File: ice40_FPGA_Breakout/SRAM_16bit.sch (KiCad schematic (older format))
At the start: 23 parts

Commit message: post review fix
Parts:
- added R?: 0, symbol R
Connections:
- net FLASH_~WP: now also R?.1; no longer R?.2, U?.3 (~WP)
- new net: R?.2, R?.2, U?.3 (~WP)
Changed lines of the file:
@@
 $EndComp
 Wire Wire Line
-	9800 3300 10100 3300
-Wire Wire Line
-	7450 3400 7950 3400
+	9800 3300 9950 3300
+Wire Wire Line
+	9950 3300 10100 3300
+Wire Wire Line
+	7450 3400 7700 3400
+Wire Wire Line
+	7700 3400 7850 3400
+Wire Wire Line
+	7850 3400 7950 3400
 Wire Wire Line
 	7550 3000 7550 3200
@@
 	7850 2550 7850 2700
 Wire Wire Line
-	7550 2550 10650 2550
+	7550 2550 7700 2550
+Wire Wire Line
+	7700 2550 7850 2550
+Wire Wire Line
+	7850 2550 9950 2550
+Wire Wire Line
+	9950 2550 10100 2550
+Wire Wire Line
+	10100 2550 10300 2550
+Wire Wire Line
+	10300 2550 10550 2550
+Wire Wire Line
+	10550 2550 10650 2550
 Connection ~ 7700 2550
 Connection ~ 9950 2550
@@
 	10300 2900 10300 2950
 Wire Wire Line
-	10300 2950 10750 2950
+	10300 2950 10550 2950
+Wire Wire Line
+	10550 2950 10750 2950
 Wire Wire Line
 	10550 2950 10550 2900
@@
 Connection ~ 10550 2950
 Wire Wire Line
-	8000 1550 8750 1550
-Wire Wire Line
-	8000 1650 8750 1650
-Wire Wire Line
-	8000 1750 8750 1750
+	8000 1550 8400 1550
+Wire Wire Line
+	8400 1550 8500 1550
+Wire Wire Line
+	8500 1550 8750 1550
+Wire Wire Line
+	8000 1650 8250 1650
+Wire Wire Line
+	8250 1650 8750 1650
+Wire Wire Line
+	8000 1750 8100 1750
+Wire Wire Line
+	8100 1750 8750 1750
 Wire Wire Line
 	8400 1200 8400 1550
 Connection ~ 8400 1550
-Wire Wire Line
-	9550 1650 10150 1650
 Connection ~ 8100 1750
 Connection ~ 8250 1650
@@
 Wire Wire Line
 	8100 1200 8100 1750
-Wire Wire Line
-	9550 1550 10150 1550
 Wire Wire Line
 	9700 1200 9700 1550
@@
 	10000 800  10000 900
 Wire Wire Line
-	7750 800  10000 800
+	7750 800  8100 800
+Wire Wire Line
+	8100 800  8250 800
+Wire Wire Line
+	8250 800  8400 800
+Wire Wire Line
+	8400 800  8700 800
+Wire Wire Line
+	8700 800  9150 800
+Wire Wire Line
+	9150 800  9350 800
+Wire Wire Line
+	9350 800  9700 800
+Wire Wire Line
+	9700 800  9850 800
+Wire Wire Line
+	9850 800  10000 800
 Wire Wire Line
 	9850 800  9850 900
@@
 	1850 3600 2000 3600
 Wire Wire Line
-	9800 3200 10150 3200
-Wire Wire Line
-	9550 1750 10150 1750
+	9800 3200 9950 3200
+Wire Wire Line
+	9950 3200 10150 3200
+Wire Wire Line
+	9550 1750 10000 1750
+Wire Wire Line
+	10000 1750 10150 1750
 Wire Wire Line
 	10000 1200 10000 1750
 Wire Wire Line
-	7450 3300 7950 3300
-Wire Wire Line
-	7450 3200 7950 3200
+	7450 3300 7700 3300
+Wire Wire Line
+	7700 3300 7950 3300
+Wire Wire Line
+	7450 3200 7550 3200
+Wire Wire Line
+	7550 3200 7950 3200
 $Comp
 L GND #PWR016
@@
 Text HLabel 10150 3200 2    39   Input Italic 8
 FPGA_SS
-Text Notes 10900 3300 2    39   Italic 8
+Text Notes 8950 3000 2    39   Italic 8
 iCE SPI SS
 Text HLabel 1850 3600 0    39   Input Italic 8
@@
 Text HLabel 1850 7350 0    39   Input Italic 8
 CMOS_CLK2
-Text HLabel 750  4450 0    39   Input Italic 8
+Text HLabel 750  4450 0    39   Input ~ 0
 LED1
-Text HLabel 750  4550 0    39   Input Italic 8
+Text HLabel 750  4550 0    39   Input ~ 0
 LED2
-Text HLabel 750  4650 0    39   Input Italic 8
+Text HLabel 750  4650 0    39   Input ~ 0
 LED3
-Text HLabel 750  4750 0    39   Input Italic 8
+Text HLabel 750  4750 0    39   Input ~ 0
 LED4
-Text HLabel 750  4850 0    39   Input Italic 8
+Text HLabel 750  4850 0    39   Input ~ 0
 LED5
-Text HLabel 750  4950 0    39   Input Italic 8
+Text HLabel 750  4950 0    39   Input ~ 0
 LED6
-Text HLabel 750  5050 0    39   Input Italic 8
+Text HLabel 750  5050 0    39   Input ~ 0
 LED7
-Text HLabel 750  4350 0    39   Input Italic 8
+Text HLabel 750  4350 0    39   Input ~ 0
 LED0
 $Comp
@@
 Text HLabel 900  5300 0    39   Input ~ 0
 XTAL2_EN
-Text GLabel 10150 1550 2    39   Input ~ 0
-FLASH_~WP
-Text GLabel 10150 1650 2    39   Input ~ 0
-FLASH_~HOLD
 Text GLabel 900  5450 0    39   Input ~ 0
 FLASH_~WP
 Text GLabel 900  5550 0    39   Input ~ 0
 FLASH_~HOLD
+Text HLabel 750  5150 0    39   Input ~ 0
+LED8
+Wire Wire Line
+	9550 1650 9850 1650
+Wire Wire Line
+	9850 1650 10800 1650
+$Comp
+L R R?
+U 1 1 5A5FCC87
+P 10250 1550
+F 0 "R?" V 10330 1550 50  0000 C CNN
+F 1 "0" V 10250 1550 50  0000 C CNN
+F 2 "" V 10180 1550 50  0001 C CNN
+F 3 "" H 10250 1550 50  0001 C CNN
+	1    10250 1550
+	0    1    -1   0
+$EndComp
+Wire Wire Line
+	9550 1550 9700 1550
+Wire Wire Line
+	9700 1550 10100 1550
+Wire Wire Line
+	10400 1550 10800 1550
+Text Label 10450 1550 0    39   ~ 0
+FLASH_~WP
+Connection ~ 10800 1550
+Text Label 10400 1650 0    39   ~ 0
+FLASH_~HOLD
+Connection ~ 10800 1650
 $EndSCHEMATC

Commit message: Component Annotated and R/C/Conn/TP CVPCB mapping
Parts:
- C19: renamed from C?; value C -> 0.1uF
- C20: renamed from C?; value C -> 1uF
- C57, C74: renamed from 0.1uf; value C -> 0.1uF
- gave numbers to parts that had none: 18
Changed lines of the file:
@@
 P 8150 3050
 AR Path="/5A0778ED/5A3EF3FF" Ref="U?"  Part="6"
-AR Path="/5A07796D/5A3EF3FF" Ref="U?"  Part="6"
-F 0 "U?" H 8250 3150 60  0000 C CNN
+AR Path="/5A07796D/5A3EF3FF" Ref="U1"  Part="6"
+F 0 "U1" H 8250 3150 60  0000 C CNN
 F 1 "iCE40HX8_CT256" H 8850 3000 60  0000 C CNN
 F 2 "" H 8150 3050 60  0001 C CNN
@@
 $EndComp
 $Comp
-L iCE40HX8_CT256 U?
+L iCE40HX8_CT256 U1
 U 2 1 5A3F10D7
 P 2200 650
-F 0 "U?" H 2300 750 60  0000 C CNN
+F 0 "U1" H 2300 750 60  0000 C CNN
 F 1 "iCE40HX8_CT256" H 2900 550 60  0000 C CNN
 F 2 "" H 2200 650 60  0001 C CNN
@@
 $EndComp
 $Comp
-L iCE40HX8_CT256 U?
+L iCE40HX8_CT256 U1
 U 3 1 5A3F1322
 P 2200 4300
-F 0 "U?" H 2300 4400 60  0000 C CNN
+F 0 "U1" H 2300 4400 60  0000 C CNN
 F 1 "iCE40HX8_CT256" H 2900 4200 60  0000 C CNN
 F 2 "" H 2200 4300 60  0001 C CNN
@@
 $EndComp
 $Comp
-L R R?
+L R R88
 U 1 1 5A3F7BB8
 P 7700 2850
-F 0 "R?" V 7780 2850 50  0000 C CNN
+F 0 "R88" V 7780 2850 50  0000 C CNN
 F 1 "DNP" V 7700 2850 50  0000 C CNN
 F 2 "" V 7630 2850 50  0001 C CNN
@@
 $EndComp
 $Comp
-L R R?
+L R R90
 U 1 1 5A3F7C81
 P 7850 2850
-F 0 "R?" V 7930 2850 50  0000 C CNN
+F 0 "R90" V 7930 2850 50  0000 C CNN
 F 1 "10K" V 7850 2850 50  0000 C CNN
 F 2 "" V 7780 2850 50  0001 C CNN
@@
 $EndComp
 $Comp
-L R R?
+L R R87
 U 1 1 5A3F7CA8
 P 7550 2850
-F 0 "R?" V 7630 2850 50  0000 C CNN
+F 0 "R87" V 7630 2850 50  0000 C CNN
 F 1 "DNP" V 7550 2850 50  0000 C CNN
 F 2 "" V 7480 2850 50  0001 C CNN
@@
 $EndComp
 $Comp
-L R R?
+L R R97
 U 1 1 5A3F7DCD
 P 9950 2800
-F 0 "R?" V 10030 2800 50  0000 C CNN
+F 0 "R97" V 10030 2800 50  0000 C CNN
 F 1 "10K" V 9950 2800 50  0000 C CNN
 F 2 "" V 9880 2800 50  0001 C CNN
@@
 $EndComp
 $Comp
-L C 0.1uf
+L C C57
 U 1 1 5A3F8150
 P 9950 3550
-F 0 "0.1uf" H 9975 3650 50  0000 L CNN
-F 1 "C" H 9975 3450 50  0000 L CNN
+F 0 "C57" H 9975 3650 50  0000 L CNN
+F 1 "0.1uF" H 9975 3450 50  0000 L CNN
 F 2 "" H 9988 3400 50  0001 C CNN
 F 3 "" H 9950 3550 50  0001 C CNN
@@
 $EndComp
 $Comp
-L C C?
+L C C19
 U 1 1 5A42CA88
 P 10300 2750
-F 0 "C?" H 10325 2850 50  0000 L CNN
-F 1 "C" H 10325 2650 50  0000 L CNN
+F 0 "C19" H 10325 2850 50  0000 L CNN
+F 1 "0.1uF" H 10325 2650 50  0000 L CNN
 F 2 "" H 10338 2600 50  0001 C CNN
 F 3 "" H 10300 2750 50  0001 C CNN
@@
 $EndComp
 $Comp
-L C C?
+L C C20
 U 1 1 5A42CAE0
 P 10550 2750
-F 0 "C?" H 10575 2850 50  0000 L CNN
-F 1 "C" H 10575 2650 50  0000 L CNN
+F 0 "C20" H 10575 2850 50  0000 L CNN
+F 1 "1uF" H 10575 2650 50  0000 L CNN
 F 2 "" H 10588 2600 50  0001 C CNN
 F 3 "" H 10550 2750 50  0001 C CNN
@@
 $EndComp
 $Comp
-L AT25_EEPROM U?
+L AT25_EEPROM U2
 U 1 1 5A2D7B12
 P 9150 1650
-F 0 "U?" H 8850 1900 50  0000 L CNN
+F 0 "U2" H 8850 1900 50  0000 L CNN
 F 1 "AT25_EEPROM" H 9200 1400 50  0000 L CNN
 F 2 "" H 8800 1600 50  0001 C CNN
@@
 $EndComp
 $Comp
-L R R?
+L R R98
 U 1 1 5A2D7D6D
 P 10000 1050
-F 0 "R?" V 10080 1050 50  0000 C CNN
+F 0 "R98" V 10080 1050 50  0000 C CNN
 F 1 "10K" V 10000 1050 50  0000 C CNN
 F 2 "" V 9930 1050 50  0001 C CNN
@@
 $EndComp
 $Comp
-L R R?
+L R R93
 U 1 1 5A2D7F27
 P 8400 1050
-F 0 "R?" V 8480 1050 50  0000 C CNN
+F 0 "R93" V 8480 1050 50  0000 C CNN
 F 1 "10K" V 8400 1050 50  0000 C CNN
 F 2 "" V 8330 1050 50  0001 C CNN
@@
 $EndComp
 $Comp
-L R R?
+L R R96
 U 1 1 5A2D84A2
 P 9850 1050
-F 0 "R?" V 9930 1050 50  0000 C CNN
+F 0 "R96" V 9930 1050 50  0000 C CNN
 F 1 "10K" V 9850 1050 50  0000 C CNN
 F 2 "" V 9780 1050 50  0001 C CNN
@@
 $EndComp
 $Comp
-L R R?
+L R R91
 U 1 1 5A2D8006
 P 8100 1050
-F 0 "R?" V 8180 1050 50  0000 C CNN
+F 0 "R91" V 8180 1050 50  0000 C CNN
 F 1 "DNP" V 8100 1050 50  0000 C CNN
 F 2 "" V 8030 1050 50  0001 C CNN
@@
 $EndComp
 $Comp
-L R R?
+L R R92
 U 1 1 5A2D7FBE
 P 8250 1050
-F 0 "R?" V 8330 1050 50  0000 C CNN
+F 0 "R92" V 8330 1050 50  0000 C CNN
 F 1 "DNP" V 8250 1050 50  0000 C CNN
 F 2 "" V 8180 1050 50  0001 C CNN
@@
 $EndComp
 $Comp
-L R R?
+L R R95
 U 1 1 5A2D8CAB
 P 9700 1050
-F 0 "R?" V 9780 1050 50  0000 C CNN
+F 0 "R95" V 9780 1050 50  0000 C CNN
 F 1 "10K" V 9700 1050 50  0000 C CNN
 F 2 "" V 9630 1050 50  0001 C CNN
@@
 $EndComp
 $Comp
-L C C?
+L C C18
 U 1 1 5A2D9A35
 P 8700 1050
-F 0 "C?" H 8725 1150 50  0000 L CNN
+F 0 "C18" H 8725 1150 50  0000 L CNN
 F 1 "0.1uf" H 8725 950 50  0000 L CNN
 F 2 "" H 8738 900 50  0001 C CNN
@@
 $EndComp
 $Comp
-L R R?
+L R R89
 U 1 1 5A2DC3A7
 P 7700 3650
-F 0 "R?" V 7780 3650 50  0000 C CNN
+F 0 "R89" V 7780 3650 50  0000 C CNN
 F 1 "DNP" V 7700 3650 50  0000 C CNN
 F 2 "" V 7630 3650 50  0001 C CNN
@@
 $EndComp
 $Comp
-L R R?
+L R R94
 U 1 1 5A2DC83D
 P 8500 2000
-F 0 "R?" V 8580 2000 50  0000 C CNN
+F 0 "R94" V 8580 2000 50  0000 C CNN
 F 1 "DNP" V 8500 2000 50  0000 C CNN
 F 2 "" V 8430 2000 50  0001 C CNN
@@
 $EndComp
 Wire Wire Line
-	9800 3300 9950 3300
-Wire Wire Line
-	9950 3300 10100 3300
-Wire Wire Line
-	7450 3400 7700 3400
-Wire Wire Line
-	7700 3400 7850 3400
-Wire Wire Line
-	7850 3400 7950 3400
+	9800 3300 10100 3300
+Wire Wire Line
+	7450 3400 7950 3400
 Wire Wire Line
 	7550 3000 7550 3200
@@
 	7850 2550 7850 2700
 Wire Wire Line
-	7550 2550 7700 2550
-Wire Wire Line
-	7700 2550 7850 2550
-Wire Wire Line
-	7850 2550 9950 2550
-Wire Wire Line
-	9950 2550 10100 2550
-Wire Wire Line
-	10100 2550 10300 2550
-Wire Wire Line
-	10300 2550 10550 2550
-Wire Wire Line
-	10550 2550 10650 2550
+	7550 2550 10650 2550
 Connection ~ 7700 2550
 Connection ~ 9950 2550
@@
 	10300 2900 10300 2950
 Wire Wire Line
-	10300 2950 10550 2950
-Wire Wire Line
-	10550 2950 10750 2950
+	10300 2950 10750 2950
 Wire Wire Line
 	10550 2950 10550 2900
@@
 Connection ~ 10550 2950
 Wire Wire Line
-	8000 1550 8400 1550
-Wire Wire Line
-	8400 1550 8500 1550
-Wire Wire Line
-	8500 1550 8750 1550
-Wire Wire Line
-	8000 1650 8250 1650
-Wire Wire Line
-	8250 1650 8750 1650
-Wire Wire Line
-	8000 1750 8100 1750
-Wire Wire Line
-	8100 1750 8750 1750
+	8000 1550 8750 1550
+Wire Wire Line
+	8000 1650 8750 1650
+Wire Wire Line
+	8000 1750 8750 1750
 Wire Wire Line
 	8400 1200 8400 1550
@@
 	10000 800  10000 900
 Wire Wire Line
-	7750 800  8100 800
-Wire Wire Line
-	8100 800  8250 800
-Wire Wire Line
-	8250 800  8400 800
-Wire Wire Line
-	8400 800  8700 800
-Wire Wire Line
-	8700 800  9150 800
-Wire Wire Line
-	9150 800  9350 800
-Wire Wire Line
-	9350 800  9700 800
-Wire Wire Line
-	9700 800  9850 800
-Wire Wire Line
-	9850 800  10000 800
+	7750 800  10000 800
 Wire Wire Line
 	9850 800  9850 900
@@
 	1850 3600 2000 3600
 Wire Wire Line
-	9800 3200 9950 3200
-Wire Wire Line
-	9950 3200 10150 3200
-Wire Wire Line
-	9550 1750 10000 1750
-Wire Wire Line
-	10000 1750 10150 1750
+	9800 3200 10150 3200
+Wire Wire Line
+	9550 1750 10150 1750
 Wire Wire Line
 	10000 1200 10000 1750
 Wire Wire Line
-	7450 3300 7700 3300
-Wire Wire Line
-	7700 3300 7950 3300
-Wire Wire Line
-	7450 3200 7550 3200
-Wire Wire Line
-	7550 3200 7950 3200
+	7450 3300 7950 3300
+Wire Wire Line
+	7450 3200 7950 3200
 $Comp
 L GND #PWR016
@@
 	2000 3700 1850 3700
 $Comp
-L Test_Point TP?
+L Test_Point TP9
 U 1 1 5A2EC2CF
 P 1850 3700
-F 0 "TP?" V 1850 4000 50  0000 C CNN
+F 0 "TP9" V 1850 4000 50  0000 C CNN
 F 1 "PLL CLK1 OUT" V 1850 4500 50  0000 C CNN
 F 2 "" H 2050 3700 50  0001 C CNN
@@
 $EndComp
 $Comp
-L Test_Point TP?
+L Test_Point TP10
 U 1 1 5A2EC7E0
 P 1850 7450
-F 0 "TP?" V 1850 7750 50  0000 C CNN
+F 0 "TP10" V 1850 7750 50  0000 C CNN
 F 1 "PLL CLK2 OUT" V 1850 8250 50  0000 C CNN
 F 2 "" H 2050 7450 50  0001 C CNN
@@
 $EndComp
 $Comp
-L C 0.1uf
+L C C74
 U 1 1 5A2FB1B9
 P 9350 1000
-F 0 "0.1uf" H 9375 1100 50  0000 L CNN
-F 1 "C" H 9375 900 50  0000 L CNN
+F 0 "C74" H 9375 1100 50  0000 L CNN
+F 1 "0.1uF" H 9375 900 50  0000 L CNN
 F 2 "" H 9388 850 50  0001 C CNN
 F 3 "" H 9350 1000 50  0001 C CNN
@@
 LED8
 Wire Wire Line
-	9550 1650 9850 1650
-Wire Wire Line
-	9850 1650 10800 1650
-$Comp
-L R R?
+	9550 1650 10800 1650
+$Comp
+L R R99
 U 1 1 5A5FCC87
 P 10250 1550
-F 0 "R?" V 10330 1550 50  0000 C CNN
+F 0 "R99" V 10330 1550 50  0000 C CNN
 F 1 "0" V 10250 1550 50  0000 C CNN
 F 2 "" V 10180 1550 50  0001 C CNN
@@
 $EndComp
 Wire Wire Line
-	9550 1550 9700 1550
-Wire Wire Line
-	9700 1550 10100 1550
+	9550 1550 10100 1550
 Wire Wire Line
 	10400 1550 10800 1550

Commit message: schematic clean up, label aligned
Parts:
- C18, C19, C57, C74: footprint (none) -> Capacitor_SMD:C_0402_1005Metric
- C20: footprint (none) -> Capacitor_SMD:C_0603_1608Metric
- R87, R88, R89, R90, R91, R92, R93, R94, R95, R96, R97, R98, R99: footprint (none) -> Resistor_SMD:R_0402_1005Metric
- TP10, TP9: footprint (none) -> Conn_PinHeader_2.00mm:PinHeader_1x01_P2.00mm_Vertical
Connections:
- net GND: now also R94.2
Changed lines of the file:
@@
 U 1 1 5A3F7BB8
 P 7700 2850
-F 0 "R88" V 7780 2850 50  0000 C CNN
+F 0 "R88" V 7650 2650 50  0000 C CNN
 F 1 "DNP" V 7700 2850 50  0000 C CNN
-F 2 "" V 7630 2850 50  0001 C CNN
+F 2 "Resistor_SMD:R_0402_1005Metric" V 7630 2850 50  0001 C CNN
 F 3 "" H 7700 2850 50  0001 C CNN
 	1    7700 2850
@@
 U 1 1 5A3F7C81
 P 7850 2850
-F 0 "R90" V 7930 2850 50  0000 C CNN
+F 0 "R90" V 7800 2650 50  0000 C CNN
 F 1 "10K" V 7850 2850 50  0000 C CNN
-F 2 "" V 7780 2850 50  0001 C CNN
+F 2 "Resistor_SMD:R_0402_1005Metric" V 7780 2850 50  0001 C CNN
 F 3 "" H 7850 2850 50  0001 C CNN
 	1    7850 2850
@@
 U 1 1 5A3F7CA8
 P 7550 2850
-F 0 "R87" V 7630 2850 50  0000 C CNN
+F 0 "R87" V 7500 2650 50  0000 C CNN
 F 1 "DNP" V 7550 2850 50  0000 C CNN
-F 2 "" V 7480 2850 50  0001 C CNN
+F 2 "Resistor_SMD:R_0402_1005Metric" V 7480 2850 50  0001 C CNN
 F 3 "" H 7550 2850 50  0001 C CNN
 	1    7550 2850
@@
 U 1 1 5A3F7DCD
 P 9950 2800
-F 0 "R97" V 10030 2800 50  0000 C CNN
+F 0 "R97" V 9900 2600 50  0000 C CNN
 F 1 "10K" V 9950 2800 50  0000 C CNN
-F 2 "" V 9880 2800 50  0001 C CNN
+F 2 "Resistor_SMD:R_0402_1005Metric" V 9880 2800 50  0001 C CNN
 F 3 "" H 9950 2800 50  0001 C CNN
 	1    9950 2800
@@
 F 0 "C57" H 9975 3650 50  0000 L CNN
 F 1 "0.1uF" H 9975 3450 50  0000 L CNN
-F 2 "" H 9988 3400 50  0001 C CNN
+F 2 "Capacitor_SMD:C_0402_1005Metric" H 9988 3400 50  0001 C CNN
 F 3 "" H 9950 3550 50  0001 C CNN
 	1    9950 3550
@@
 F 0 "C19" H 10325 2850 50  0000 L CNN
 F 1 "0.1uF" H 10325 2650 50  0000 L CNN
-F 2 "" H 10338 2600 50  0001 C CNN
+F 2 "Capacitor_SMD:C_0402_1005Metric" H 10338 2600 50  0001 C CNN
 F 3 "" H 10300 2750 50  0001 C CNN
 	1    10300 2750
@@
 F 0 "C20" H 10575 2850 50  0000 L CNN
 F 1 "1uF" H 10575 2650 50  0000 L CNN
-F 2 "" H 10588 2600 50  0001 C CNN
+F 2 "Capacitor_SMD:C_0603_1608Metric" H 10588 2600 50  0001 C CNN
 F 3 "" H 10550 2750 50  0001 C CNN
 	1    10550 2750
@@
 P 9150 1650
 F 0 "U2" H 8850 1900 50  0000 L CNN
-F 1 "AT25_EEPROM" H 9200 1400 50  0000 L CNN
+F 1 "AT25_EEPROM" H 8600 1400 50  0000 L CNN
 F 2 "" H 8800 1600 50  0001 C CNN
 F 3 "" H 8800 1600 50  0001 C CNN
@@
 U 1 1 5A2D7D6D
 P 10000 1050
-F 0 "R98" V 10080 1050 50  0000 C CNN
+F 0 "R98" V 10050 850 50  0000 C CNN
 F 1 "10K" V 10000 1050 50  0000 C CNN
-F 2 "" V 9930 1050 50  0001 C CNN
+F 2 "Resistor_SMD:R_0402_1005Metric" V 9930 1050 50  0001 C CNN
 F 3 "" H 10000 1050 50  0001 C CNN
 	1    10000 1050
@@
 U 1 1 5A2D7F27
 P 8400 1050
-F 0 "R93" V 8480 1050 50  0000 C CNN
+F 0 "R93" V 8450 850 50  0000 C CNN
 F 1 "10K" V 8400 1050 50  0000 C CNN
-F 2 "" V 8330 1050 50  0001 C CNN
+F 2 "Resistor_SMD:R_0402_1005Metric" V 8330 1050 50  0001 C CNN
 F 3 "" H 8400 1050 50  0001 C CNN
 	1    8400 1050
@@
 U 1 1 5A2D84A2
 P 9850 1050
-F 0 "R96" V 9930 1050 50  0000 C CNN
+F 0 "R96" V 9900 850 50  0000 C CNN
 F 1 "10K" V 9850 1050 50  0000 C CNN
-F 2 "" V 9780 1050 50  0001 C CNN
+F 2 "Resistor_SMD:R_0402_1005Metric" V 9780 1050 50  0001 C CNN
 F 3 "" H 9850 1050 50  0001 C CNN
 	1    9850 1050
@@
 U 1 1 5A2D8006
 P 8100 1050
-F 0 "R91" V 8180 1050 50  0000 C CNN
+F 0 "R91" V 8150 850 50  0000 C CNN
 F 1 "DNP" V 8100 1050 50  0000 C CNN
-F 2 "" V 8030 1050 50  0001 C CNN
+F 2 "Resistor_SMD:R_0402_1005Metric" V 8030 1050 50  0001 C CNN
 F 3 "" H 8100 1050 50  0001 C CNN
 	1    8100 1050
@@
 U 1 1 5A2D7FBE
 P 8250 1050
-F 0 "R92" V 8330 1050 50  0000 C CNN
+F 0 "R92" V 8300 850 50  0000 C CNN
 F 1 "DNP" V 8250 1050 50  0000 C CNN
-F 2 "" V 8180 1050 50  0001 C CNN
+F 2 "Resistor_SMD:R_0402_1005Metric" V 8180 1050 50  0001 C CNN
 F 3 "" H 8250 1050 50  0001 C CNN
 	1    8250 1050
@@
 U 1 1 5A2D8CAB
 P 9700 1050
-F 0 "R95" V 9780 1050 50  0000 C CNN
+F 0 "R95" V 9750 850 50  0000 C CNN
 F 1 "10K" V 9700 1050 50  0000 C CNN
-F 2 "" V 9630 1050 50  0001 C CNN
+F 2 "Resistor_SMD:R_0402_1005Metric" V 9630 1050 50  0001 C CNN
 F 3 "" H 9700 1050 50  0001 C CNN
 	1    9700 1050
@@
 F 0 "C18" H 8725 1150 50  0000 L CNN
 F 1 "0.1uf" H 8725 950 50  0000 L CNN
-F 2 "" H 8738 900 50  0001 C CNN
+F 2 "Capacitor_SMD:C_0402_1005Metric" H 8738 900 50  0001 C CNN
 F 3 "" H 8700 1050 50  0001 C CNN
 	1    8700 1050
@@
 F 0 "R89" V 7780 3650 50  0000 C CNN
 F 1 "DNP" V 7700 3650 50  0000 C CNN
-F 2 "" V 7630 3650 50  0001 C CNN
+F 2 "Resistor_SMD:R_0402_1005Metric" V 7630 3650 50  0001 C CNN
 F 3 "" H 7700 3650 50  0001 C CNN
 	1    7700 3650
@@
 F 0 "R94" V 8580 2000 50  0000 C CNN
 F 1 "DNP" V 8500 2000 50  0000 C CNN
-F 2 "" V 8430 2000 50  0001 C CNN
+F 2 "Resistor_SMD:R_0402_1005Metric" V 8430 2000 50  0001 C CNN
 F 3 "" H 8500 2000 50  0001 C CNN
 	1    8500 2000
@@
 Connection ~ 8500 1550
 Wire Wire Line
-	8500 2150 8500 2250
-Wire Wire Line
 	1850 3600 2000 3600
 Wire Wire Line
@@
 F 0 "TP9" V 1850 4000 50  0000 C CNN
 F 1 "PLL CLK1 OUT" V 1850 4500 50  0000 C CNN
-F 2 "" H 2050 3700 50  0001 C CNN
+F 2 "Conn_PinHeader_2.00mm:PinHeader_1x01_P2.00mm_Vertical" H 2050 3700 50  0001 C CNN
 F 3 "" H 2050 3700 50  0001 C CNN
 	1    1850 3700
@@
 F 0 "TP10" V 1850 7750 50  0000 C CNN
 F 1 "PLL CLK2 OUT" V 1850 8250 50  0000 C CNN
-F 2 "" H 2050 7450 50  0001 C CNN
+F 2 "Conn_PinHeader_2.00mm:PinHeader_1x01_P2.00mm_Vertical" H 2050 7450 50  0001 C CNN
 F 3 "" H 2050 7450 50  0001 C CNN
 	1    1850 7450
@@
 F 0 "C74" H 9375 1100 50  0000 L CNN
 F 1 "0.1uF" H 9375 900 50  0000 L CNN
-F 2 "" H 9388 850 50  0001 C CNN
+F 2 "Capacitor_SMD:C_0402_1005Metric" H 9388 850 50  0001 C CNN
 F 3 "" H 9350 1000 50  0001 C CNN
 	1    9350 1000
@@
 P 7850 950
 F 0 "#PWR018" H 7850 700 50  0001 C CNN
-F 1 "GND" H 8000 900 50  0000 C CNN
+F 1 "GND" H 7800 800 50  0000 C CNN
 F 2 "" H 7850 950 50  0001 C CNN
 F 3 "" H 7850 950 50  0001 C CNN
@@
 F 0 "R99" V 10330 1550 50  0000 C CNN
 F 1 "0" V 10250 1550 50  0000 C CNN
-F 2 "" V 10180 1550 50  0001 C CNN
+F 2 "Resistor_SMD:R_0402_1005Metric" V 10180 1550 50  0001 C CNN
 F 3 "" H 10250 1550 50  0001 C CNN
 	1    10250 1550
@@
 FLASH_~HOLD
 Connection ~ 10800 1650
+Wire Wire Line
+	8500 2200 8500 2150
 $EndSCHEMATC

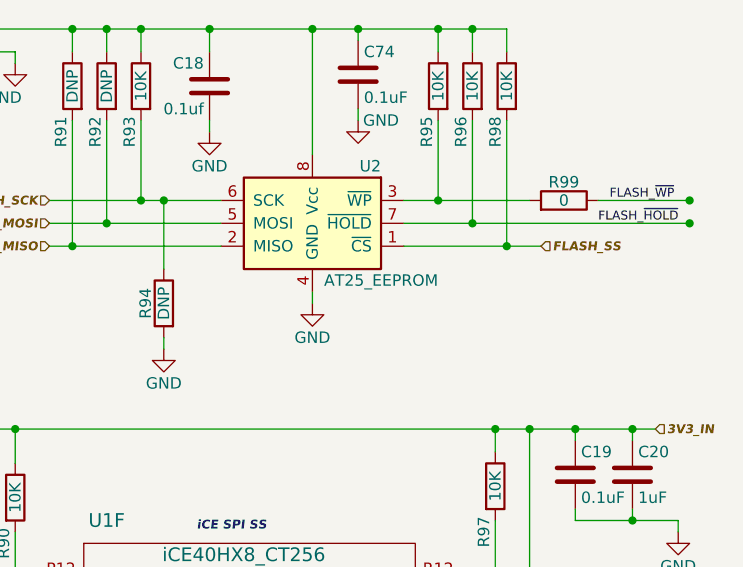
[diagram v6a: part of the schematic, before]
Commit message: assigned footprint to each component
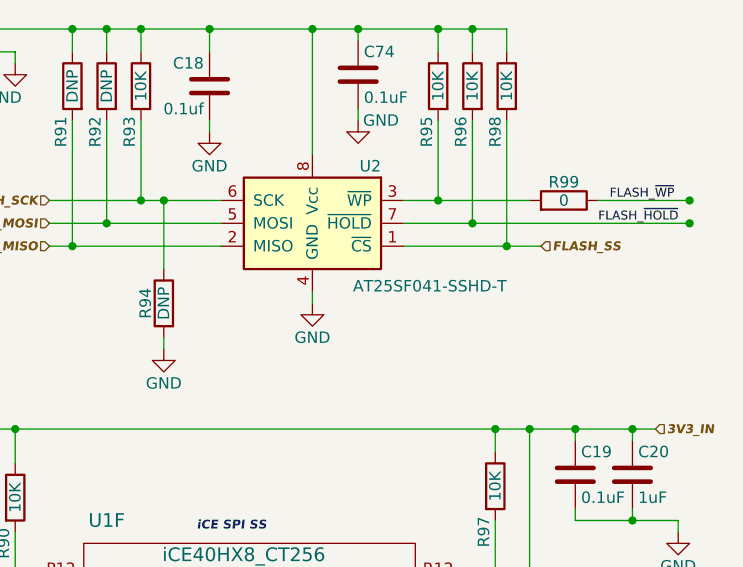
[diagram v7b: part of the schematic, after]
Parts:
- TP10, TP9: footprint Conn_PinHeader_2.00mm:PinHeader_1x01_P2.00mm_Vertical -> TestPoint:TestPoint_Pad_D2.0mm
- U1: footprint (none) -> GTI_Footprint_Lib:BGA-256_12mmx12mm_Layout_14mmx14mm_P0.8mm_R0.5mm
- U2: value AT25_EEPROM -> AT25SF041-SSHD-T; footprint (none) -> Package_SO:SOIC-8_3.9x4.9mm_P1.27mm
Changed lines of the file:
@@
 F 0 "U1" H 2300 750 60  0000 C CNN
 F 1 "iCE40HX8_CT256" H 2900 550 60  0000 C CNN
-F 2 "" H 2200 650 60  0001 C CNN
+F 2 "GTI_Footprint_Lib:BGA-256_12mmx12mm_Layout_14mmx14mm_P0.8mm_R0.5mm" H 2200 650 60  0001 C CNN
 F 3 "" H 2200 650 60  0001 C CNN
 	2    2200 650
@@
 F 0 "U1" H 2300 4400 60  0000 C CNN
 F 1 "iCE40HX8_CT256" H 2900 4200 60  0000 C CNN
-F 2 "" H 2200 4300 60  0001 C CNN
+F 2 "GTI_Footprint_Lib:BGA-256_12mmx12mm_Layout_14mmx14mm_P0.8mm_R0.5mm" H 2200 4300 60  0001 C CNN
 F 3 "" H 2200 4300 60  0001 C CNN
 	3    2200 4300
@@
 P 9150 1650
 F 0 "U2" H 8850 1900 50  0000 L CNN
-F 1 "AT25_EEPROM" H 8600 1400 50  0000 L CNN
-F 2 "" H 8800 1600 50  0001 C CNN
+F 1 " AT25SF041-SSHD-T " H 8300 1375 50  0000 L CNN
+F 2 "Package_SO:SOIC-8_3.9x4.9mm_P1.27mm" H 8800 1600 50  0001 C CNN
 F 3 "" H 8800 1600 50  0001 C CNN
 	1    9150 1650
@@
 F 0 "TP9" V 1850 4000 50  0000 C CNN
 F 1 "PLL CLK1 OUT" V 1850 4500 50  0000 C CNN
-F 2 "Conn_PinHeader_2.00mm:PinHeader_1x01_P2.00mm_Vertical" H 2050 3700 50  0001 C CNN
+F 2 "TestPoint:TestPoint_Pad_D2.0mm" H 2050 3700 50  0001 C CNN
 F 3 "" H 2050 3700 50  0001 C CNN
 	1    1850 3700
@@
 F 0 "TP10" V 1850 7750 50  0000 C CNN
 F 1 "PLL CLK2 OUT" V 1850 8250 50  0000 C CNN
-F 2 "Conn_PinHeader_2.00mm:PinHeader_1x01_P2.00mm_Vertical" H 2050 7450 50  0001 C CNN
+F 2 "TestPoint:TestPoint_Pad_D2.0mm" H 2050 7450 50  0001 C CNN
 F 3 "" H 2050 7450 50  0001 C CNN
 	1    1850 7450
